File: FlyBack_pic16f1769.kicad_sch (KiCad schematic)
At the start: 0 parts

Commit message: 绘制pic16f1769最小系统电路；
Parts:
- added J1: ICSP, Connector_PinHeader_2.54mm:PinHeader_1x06_P2.54mm_Vertical, symbol Connector_Generic:Conn_01x06
- added Rost: 1.8k, Resistor_SMD:R_0603_1608Metric_Pad0.98x0.95mm_HandSolder, symbol Device:R_Small_US
- added U1: PIC16F1769-I/P, kicad_api_lib:PIC16F1769-I_P, symbol PIC16F1769-I_P:PIC16LF1769-E_P
- added U2: MCP1416, Package_TO_SOT_SMD:SOT-23-5_HandSoldering, symbol Driver_FET:MCP1416
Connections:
- new net: Rost.2, U1.17 (RA2)
- new net +5V: J1.2 (Pin_2), U1.1 (VDD)
- new net GND: J1.3 (Pin_3), U1.20 (VSS), U2.4 (GND)
- new net GateV: U1.16 (RC0), U2.3 (IN)
- new net ICSPCLK: J1.5 (Pin_5), U1.18 (RA1)
- new net ICSPDAT: J1.4 (Pin_4), U1.19 (RA0)
- new net Isense: Rost.1, U1.15 (RC1)
- new net MCLR: J1.1 (Pin_1), U1.4 (MCLR#/VPP/RA3)
- new net OP1-: U1.13 (RB4)
- new net OP1o/Ramp: U1.11 (RB6), U1.14 (RC2)
- new net RX: U1.6 (RC4)
- new net SCL: U1.9 (RC7)
- new net SDA: U1.8 (RC6)
- new net TX: U1.5 (RC5)
- new net VFB: U1.10 (RB7), U1.7 (RC3)
- new net Vdrive: U2.2 (Vdd)
- no-connect marks 0 -> 3

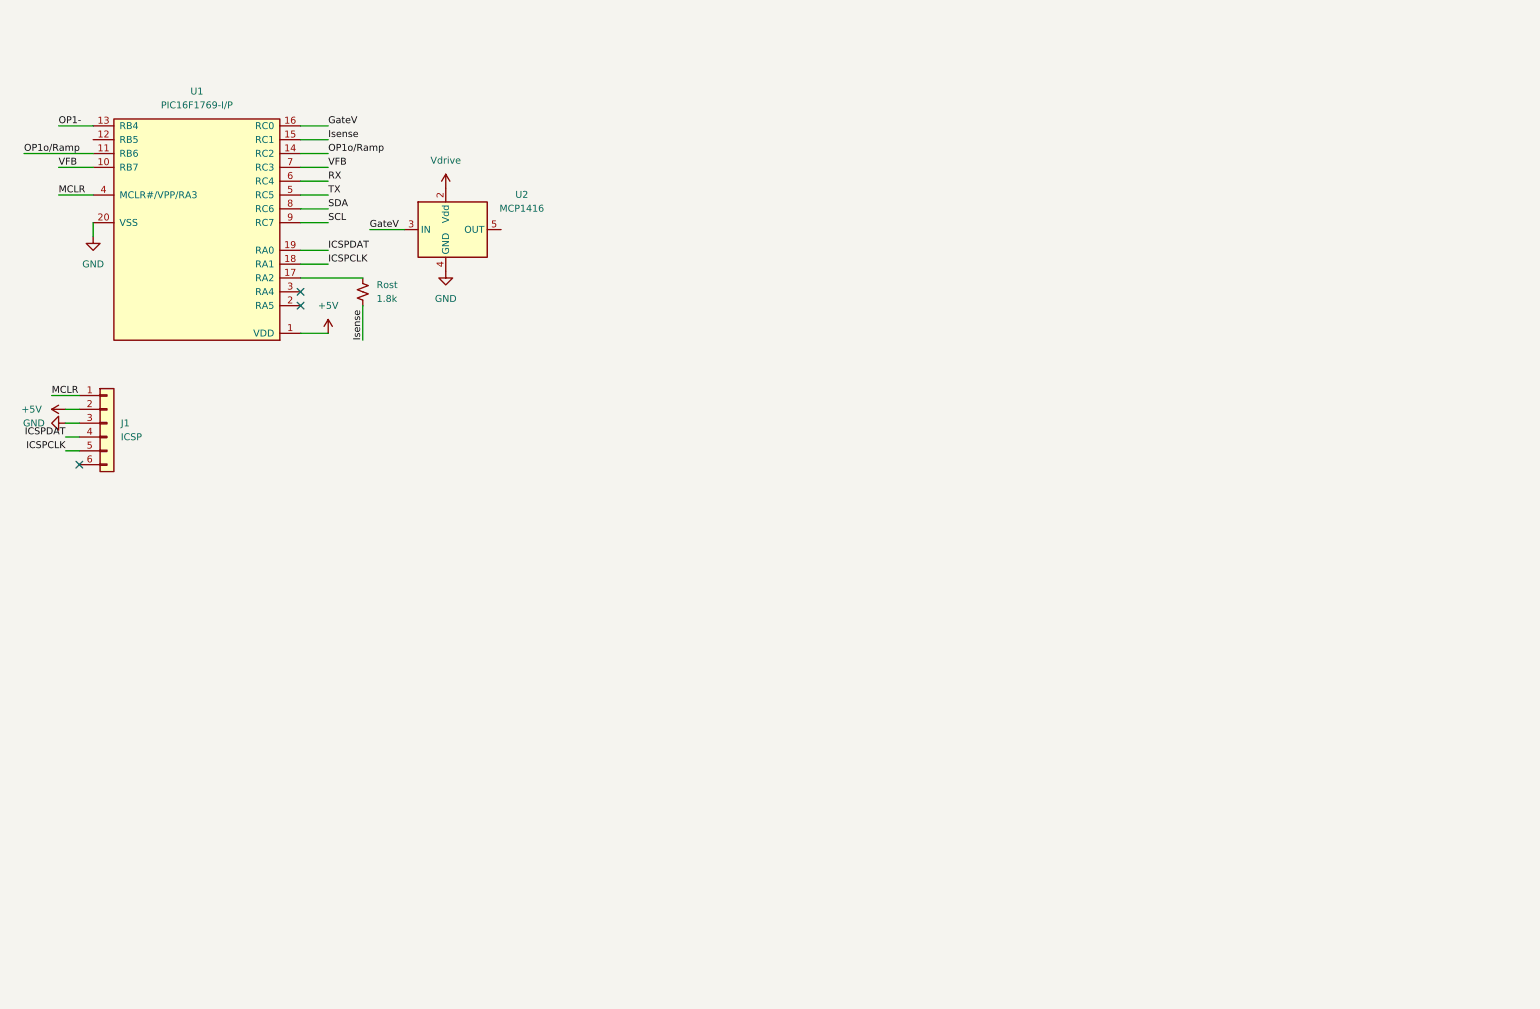
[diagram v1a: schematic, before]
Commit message: 绘制RC吸收和电流采样电路；
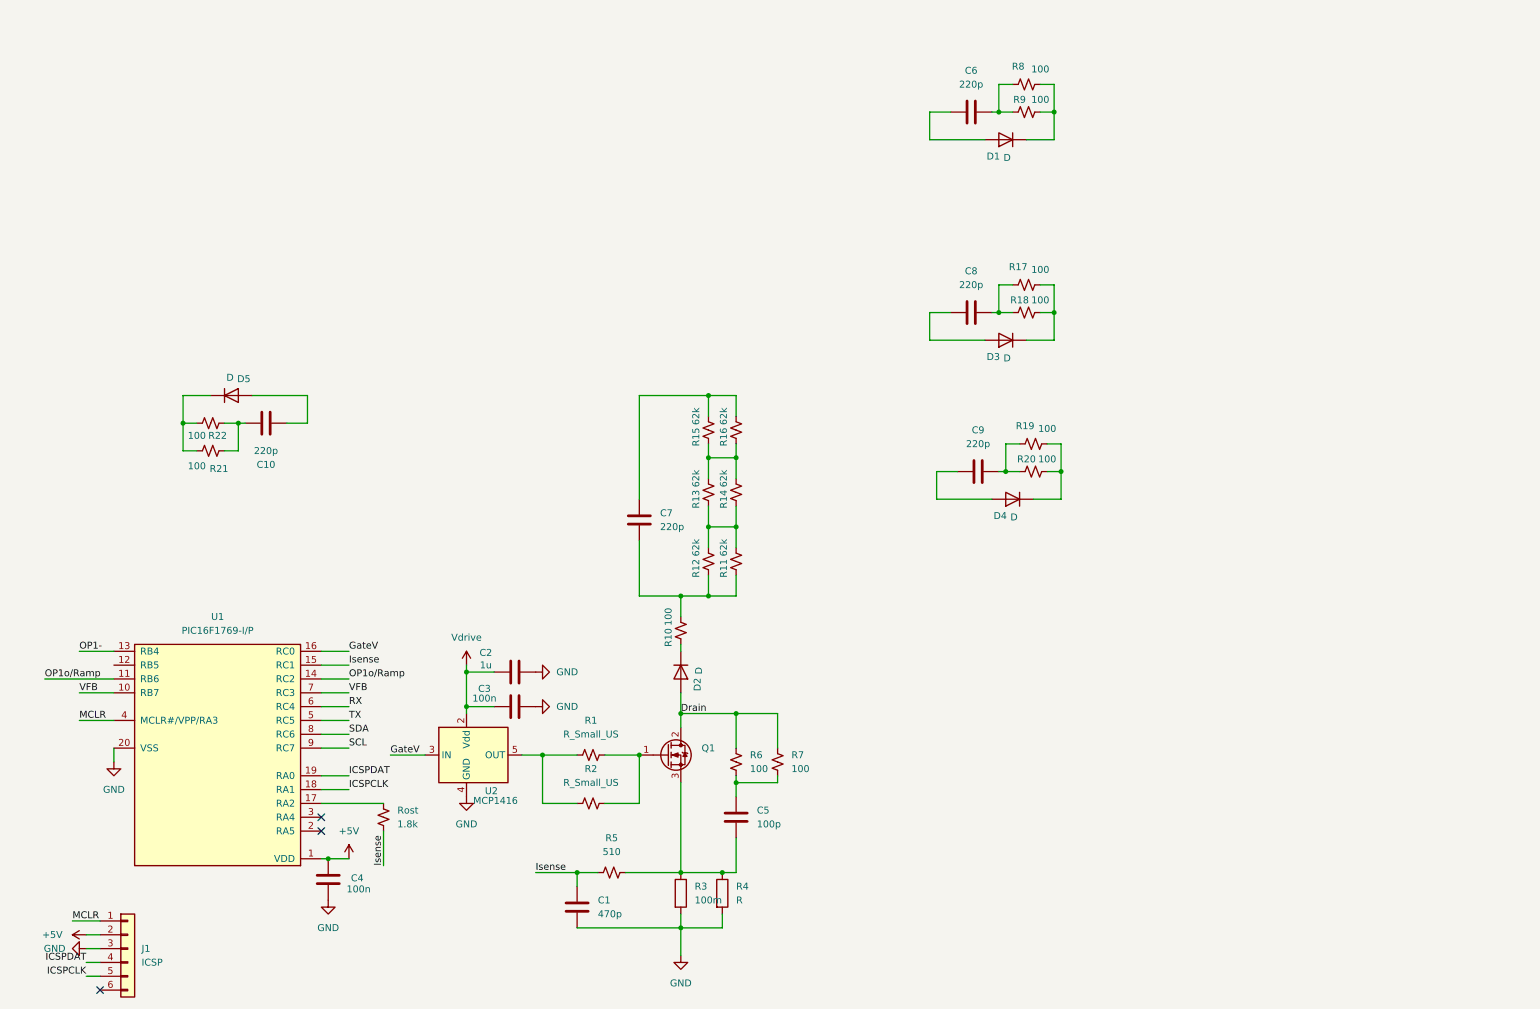
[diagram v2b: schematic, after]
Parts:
- added C1: 470p, Capacitor_SMD:C_0603_1608Metric_Pad1.08x0.95mm_HandSolder, symbol Device:C
- added C10, C6, C7, C8, C9: 220p, Capacitor_SMD:C_1206_3216Metric_Pad1.33x1.80mm_HandSolder, symbol Device:C
- added C2: 1u, Capacitor_SMD:C_0603_1608Metric_Pad1.08x0.95mm_HandSolder, symbol Device:C
- added C3, C4: 100n, Capacitor_SMD:C_0603_1608Metric_Pad1.08x0.95mm_HandSolder, symbol Device:C
- added C5: 100p, Capacitor_SMD:C_0805_2012Metric_Pad1.18x1.45mm_HandSolder, symbol Device:C
- added D1, D2, D3, D4, D5: D, Diode_SMD:D_SMB_Handsoldering, symbol Device:D
- added Q1: IPD50R380CE, Package_TO_SOT_SMD:TO-252-2, symbol Transistor_FET:IPD50R380CE
- added R1, R2: R_Small_US, Resistor_SMD:R_0805_2012Metric_Pad1.20x1.40mm_HandSolder, symbol Device:R_Small_US
- added R10, R17, R18, R19, R20, R21, R22, R6, R7, R8, R9: 100, Resistor_SMD:R_1206_3216Metric_Pad1.30x1.75mm_HandSolder, symbol Device:R_Small_US
- added R11, R12, R13, R14, R15, R16: 62k, Resistor_SMD:R_1206_3216Metric_Pad1.30x1.75mm_HandSolder, symbol Device:R_Small_US
- added R3: 100m, Resistor_SMD:R_2512_6332Metric_Pad1.40x3.35mm_HandSolder, symbol Device:R
- added R4: R, Resistor_SMD:R_2512_6332Metric_Pad1.40x3.35mm_HandSolder, symbol Device:R
- added R5: 510, Resistor_SMD:R_0603_1608Metric_Pad0.98x0.95mm_HandSolder, symbol Device:R_Small_US
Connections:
- net +5V: now also C4.2
- net GND: now also C1.2, C2.2, C3.2, C4.1, R3.2, R4.2
- net Isense: now also C1.1, R5.1
- net Vdrive: now also C2.1, C3.1
- net at U2.5 (OUT): now also R1.1, R2.1
- new net: C6.2, R8.1, R9.1
- new net: D1.1 (K), R8.2, R9.2
- new net: C7.1, R10.2, R11.1, R12.1
- new net: R11.2, R12.2, R13.1, R14.1
- new net: R13.2, R14.2, R15.1, R16.1
- new net: C7.2, R15.2, R16.2
- new net: C9.2, R19.1, R20.1
- new net: D4.1 (K), R19.2, R20.2
- new net: C10.1, D5.2 (A)
- new net: C10.2, R21.1, R22.1
- new net: C5.2, Q1.3 (S), R3.1, R4.1, R5.2
- new net: D5.1 (K), R21.2, R22.2
- new net: C5.1, R6.2, R7.2
- new net: C8.2, R17.1, R18.1
- new net: D3.1 (K), R17.2, R18.2
- new net: Q1.1 (G), R1.2, R2.2
- new net: C8.1, D3.2 (A)
- new net: D2.1 (K), R10.1
- new net: C6.1, D1.2 (A)
- new net: C9.1, D4.2 (A)
- new net Drain: D2.2 (A), Q1.2 (D), R6.1, R7.1
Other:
- moved on the sheet: J1, Rost, U1, U2

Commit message: 反激输出原理图绘制；补偿电路1原理图绘制；
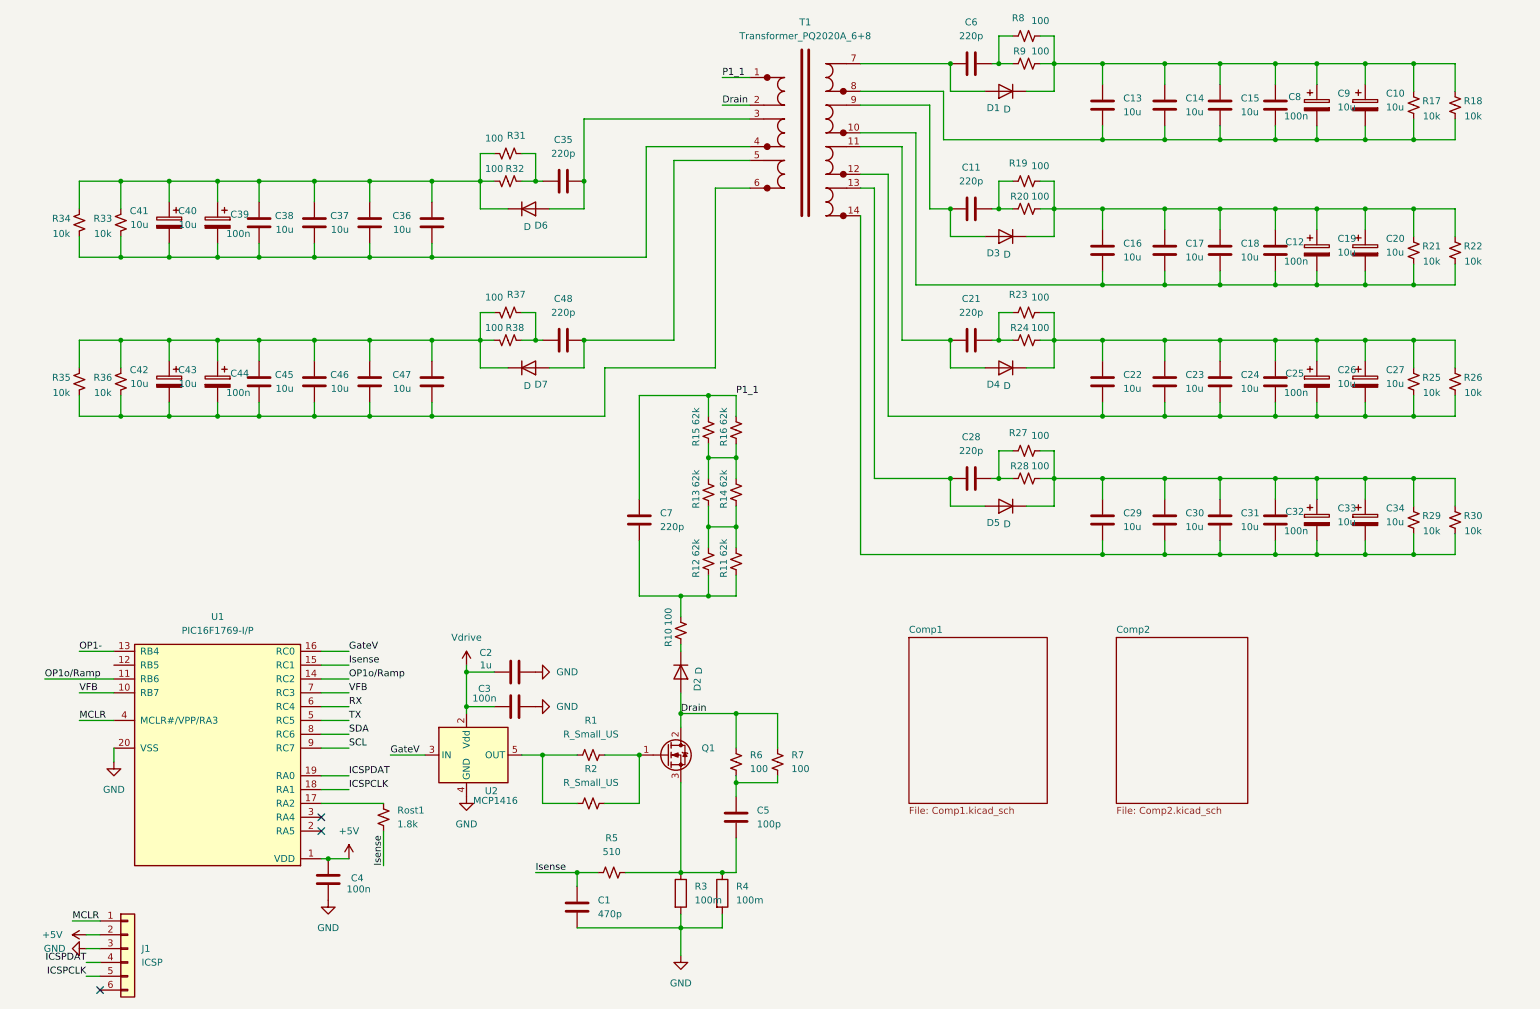
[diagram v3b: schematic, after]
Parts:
- removed C10, C9: 220p, Capacitor_SMD:C_1206_3216Metric_Pad1.33x1.80mm_HandSolder, symbol Device:C
- added C10, C19, C20, C26, C27, C33, C34, C40, C41, C42, C43, C9: 10u, Capacitor_SMD:CP_Elec_10x12.5, symbol Device:C_Polarized
- added C11, C21, C28, C35, C48: 220p, Capacitor_SMD:C_1206_3216Metric_Pad1.33x1.80mm_HandSolder, symbol Device:C
- added C12, C25, C32, C39, C44: 100n, Capacitor_SMD:C_0603_1608Metric_Pad1.08x0.95mm_HandSolder, symbol Device:C
- added C13, C14, C15, C16, C17, C18, C22, C23, C24, C29, C30, C31, C36, C37, C38, C45, C46, C47: 10u, Capacitor_SMD:C_1206_3216Metric_Pad1.33x1.80mm_HandSolder, symbol Device:C
- added D6, D7: D, Diode_SMD:D_SMB_Handsoldering, symbol Device:D
- added R23, R24, R27, R28, R31, R32, R37, R38: 100, Resistor_SMD:R_1206_3216Metric_Pad1.30x1.75mm_HandSolder, symbol Device:R_Small_US
- added R25, R26, R29, R30, R33, R34, R35, R36: 10k, Resistor_SMD:R_1206_3216Metric_Pad1.30x1.75mm_HandSolder, symbol Device:R_Small_US
- added T1: Transformer_PQ2020A_6+8, user_pretty:Transformer_PQ2020A_6+8_23x23mm, symbol Transformer_PQ2020A_6+8:Transformer_PQ2020A_6+8
- C8: value 220p -> 100n; footprint Capacitor_SMD:C_1206_3216Metric_Pad1.33x1.80mm_HandSolder -> Capacitor_SMD:C_0603_1608Metric_Pad1.08x0.95mm_HandSolder
- R17, R18, R21, R22: value 100 -> 10k
- R4: value R -> 100m
- renumbered Rost to Rost1
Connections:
- net Drain: now also T1.2
- net at D1.1 (K), R8.2, R9.2: now also C8.2, R17.2, R18.2, C10.1, C13.2, C14.2, C15.2, C9.1
- net P1_1: now reaches C7.2, R15.2, R16.2
- net P1_1: now also T1.1
- net at R19.1, R20.1: now also C11.2
- net at R19.2, R20.2: now also D3.1 (K), R21.2, R22.2, C12.2, C16.2, C17.2, C18.2, C19.1, C20.1; no longer D4.1 (K)
- net at D5.2 (A): now also C28.1, T1.13
- net at R21.1, R22.1: now also C12.1, C16.1, C17.1, C18.1, C19.2, C20.2, T1.10
- net at R17.1, R18.1: now also C8.1, C10.2, C13.1, C14.1, C15.1, C9.2, T1.8; no longer C8.2
- net at D3.2 (A): now also C11.1, T1.9; no longer C8.1
- net at C6.1, D1.2 (A): now also T1.7
- net at D4.2 (A): now also C21.1, T1.11
- new net: C36.1, C37.1, C38.1, C39.1, C40.2, C41.2, R33.1, R34.1, T1.4
- new net: C36.2, C37.2, C38.2, C39.2, C40.1, C41.1, D6.1 (K), R31.2, R32.2, R33.2, R34.2
- new net: C35.2, R31.1, R32.1
- new net: C42.1, C43.1, C44.2, C45.2, C46.2, C47.2, D7.1 (K), R35.2, R36.2, R37.2, R38.2
- new net: C48.1, D7.2 (A), T1.5
- new net: C29.1, C30.1, C31.1, C32.1, C33.2, C34.2, R29.1, R30.1, T1.14
- new net: C29.2, C30.2, C31.2, C32.2, C33.1, C34.1, D5.1 (K), R27.2, R28.2, R29.2, R30.2
- new net: C22.1, C23.1, C24.1, C25.1, C26.2, C27.2, R25.1, R26.1, T1.12
- new net: C35.1, D6.2 (A), T1.3
- new net: C42.2, C43.2, C44.1, C45.1, C46.1, C47.1, R35.1, R36.1, T1.6
- new net: C28.2, R27.1, R28.1
- new net: C22.2, C23.2, C24.2, C25.2, C26.1, C27.1, D4.1 (K), R23.2, R24.2, R25.2, R26.2
- new net: C48.2, R37.1, R38.1
- new net: C21.2, R23.1, R24.1
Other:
- added sheet Comp1 (Comp1.kicad_sch)
- added sheet Comp2 (Comp2.kicad_sch)
- moved on the sheet: C6, D1, R8, R9

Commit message: 完善补偿电路原理图；
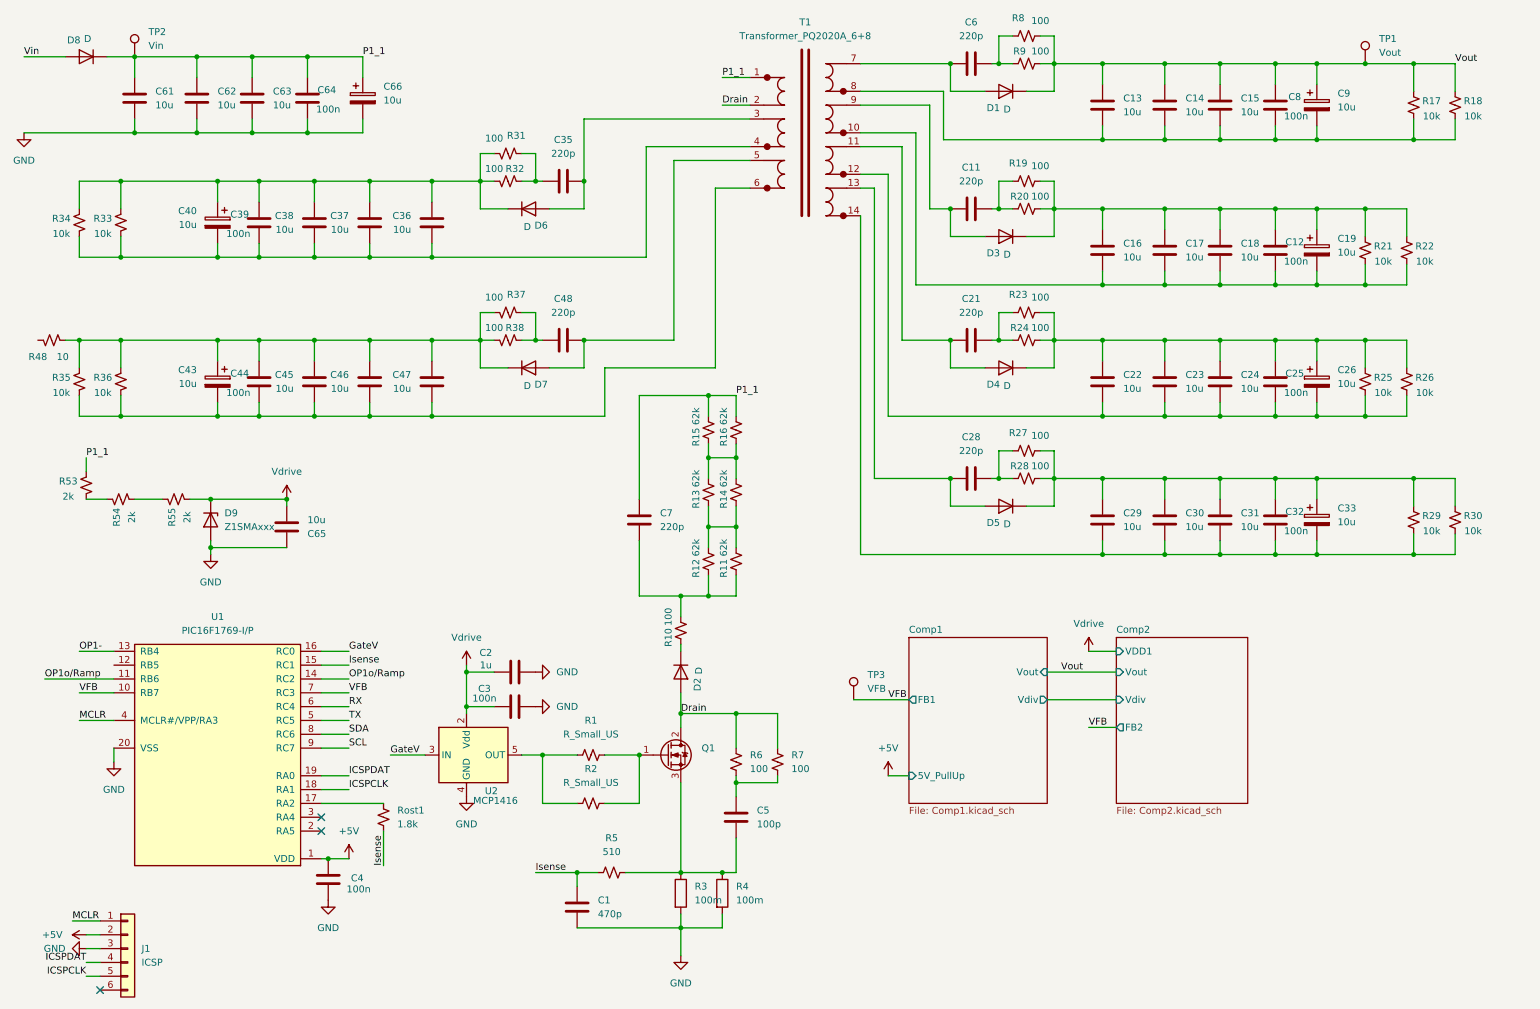
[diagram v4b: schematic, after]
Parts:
- removed C10, C20, C27, C34, C41, C42: 10u, Capacitor_SMD:CP_Elec_10x12.5, symbol Device:C_Polarized
- added C61, C62, C63, C65: 10u, Capacitor_SMD:C_1206_3216Metric_Pad1.33x1.80mm_HandSolder, symbol Device:C
- added C64: 100n, Capacitor_SMD:C_0603_1608Metric_Pad1.08x0.95mm_HandSolder, symbol Device:C
- added C66: 10u, Capacitor_SMD:CP_Elec_10x12.5, symbol Device:C_Polarized
- added D8: D, Diode_SMD:D_SMC, symbol Device:D
- added D9: Z1SMAxxx, Diode_SMD:D_SMA, symbol Diode:Z1SMAxxx
- added R48: 10, Resistor_SMD:R_1206_3216Metric_Pad1.30x1.75mm_HandSolder, symbol Device:R_Small_US
- added R53, R54, R55: 2k, Resistor_SMD:R_1206_3216Metric_Pad1.30x1.75mm_HandSolder, symbol Device:R_Small_US
- added TP1: Vout, TestPoint:TestPoint_Keystone_5005-5009_Compact, symbol Connector:TestPoint
- added TP2: Vin, TestPoint:TestPoint_Keystone_5005-5009_Compact, symbol Connector:TestPoint
- added TP3: VFB, TestPoint:TestPoint_Keystone_5005-5009_Compact, symbol Connector:TestPoint
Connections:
- net GND: now also C61.1, C62.1, C63.1, C64.1, C65.2, C66.2, D9.2 (A)
- net P1_1: now also C61.2, C62.2, C63.2, C64.2, C66.1, D8.1 (K), R53.2, TP2.1
- net VFB: now also TP3.1
- net Vdrive: now also C65.1, D9.1 (K), R55.1
- net Vout: now reaches C13.2, C14.2, C15.2, C8.2, C9.1, D1.1 (K), R17.2, R18.2, R8.2, R9.2
- net Vout: now also TP1.1
- net at C43.1, C44.2, C45.2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: now also R48.1
- new net: R54.1, R55.2
- new net: R53.1, R54.2
- new net Vin: D8.2 (A)
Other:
- sheet Comp1 ports: added 5V_PullUp, FB1, Vdiv, Vout; removed none
- sheet Comp2 ports: added FB2, VDD1, Vdiv, Vout; removed none
- moved on the sheet: R21, R22, R25, R26
